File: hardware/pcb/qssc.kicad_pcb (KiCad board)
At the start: 6 copper layers, 210 x 140 mm, 124 parts, among them J1 FT232RL, J10 USB-C, J12 BTB_HOST, J2 5V Barrel, J3 SMA, J4 12V LED, J7 RESET, J8 MW_GATE, J9 JTAG, U1 XC7A35T-1CSG324C, U3 ADF4351BCPZ, U5 GVA-84+, U8 W25Q128JVSIQ, Y1 100MHz TCXO

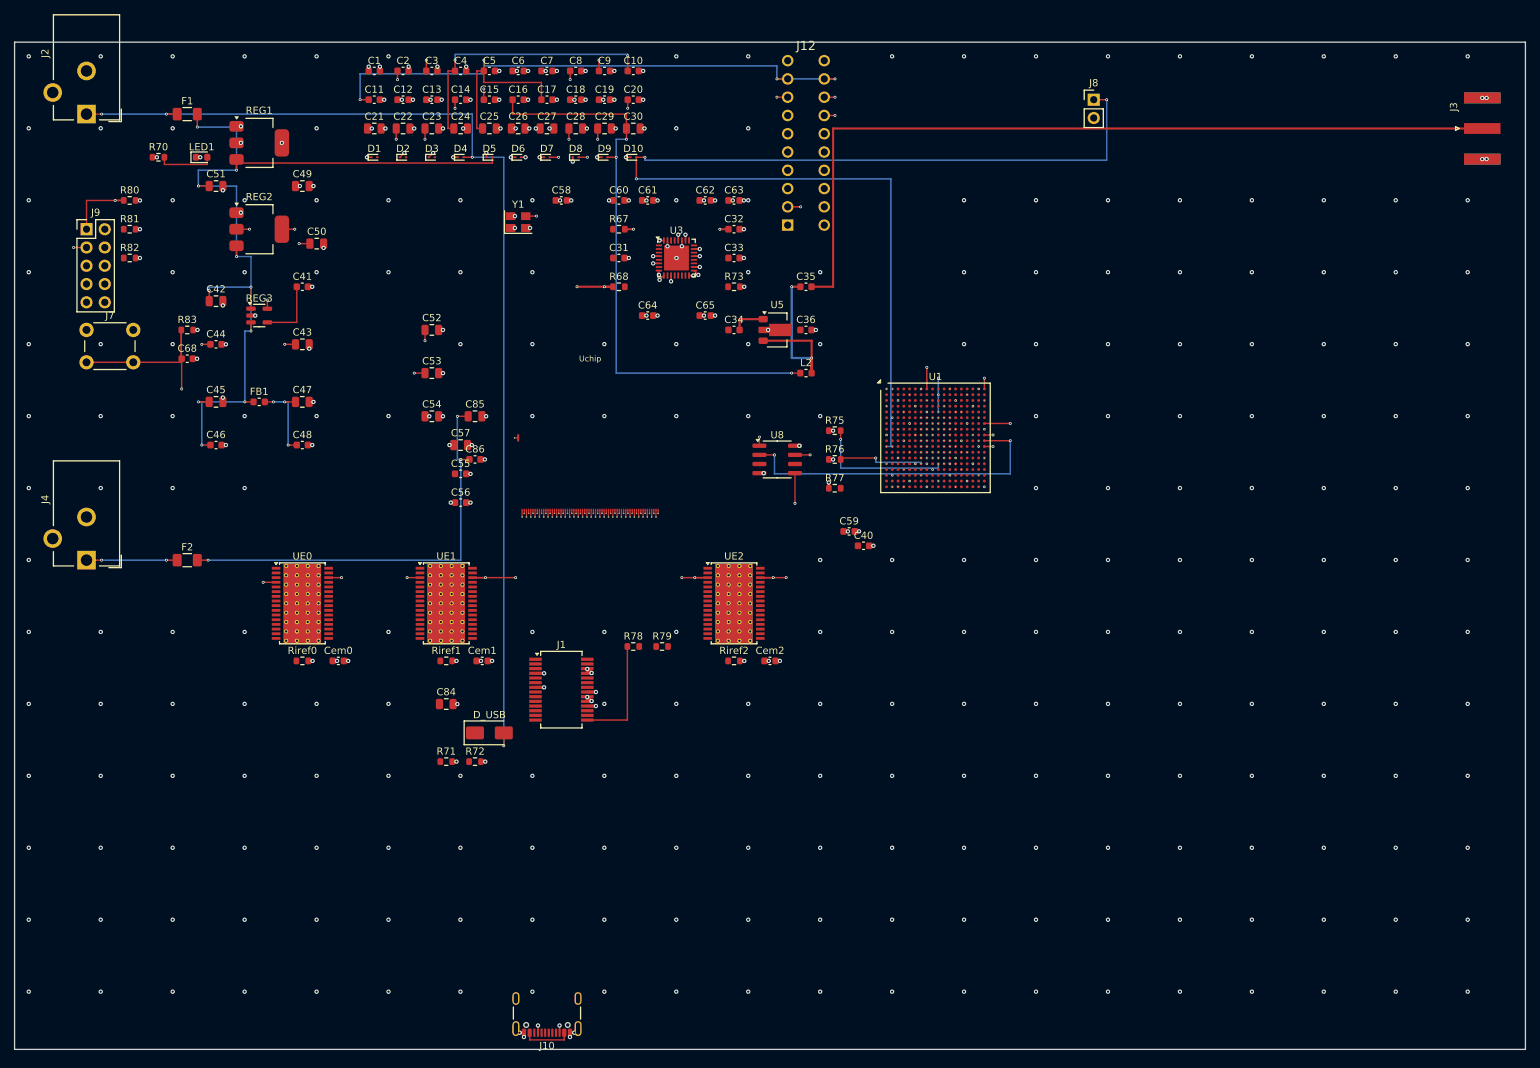
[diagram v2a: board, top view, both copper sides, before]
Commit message: pcb: Ironwood SBT socket + per-datasheet pin fixes + no_connect markers
Step 0 — Ironwood SBT open-top spring-pin socket (emitter face, main board):
  - socket_footprint(): 65 solder pads (64 EM + EM_ANODE) on F.Cu+F.Paste+F.Mask
    at the 0.30mm die-contact pitch, 4 NPTH M2 mount holes, 25x25mm body +
    courtyard. lib_id "qssc:Ironwood_SBT" + symbol; Uchip swapped from
    QSSC_Chip_EM. This is the commercial made-to-order socket that fits the
    20x20mm / 0.30mm-pitch die (no off-the-shelf socket exists at that pitch).
  - Head-board QSSC_Chip_DET (detector face) unchanged: ACF/pogo on B.Cu.

Step 1 — per-datasheet pin audit + (no_connect) emission (addresses
"practically nothing connected per its datasheet"):
  - FT232RL: net pin 24 -> +3V3 (VCC) and pin 23 -> GND (AGND) -- both required
    supply/ground pads per SSOP-28 that were previously unnetted.
  - ADF4351: REFIN- (pin 19) decoupled to GND via new C37 100nF (single-ended
    CMOS ref, datasheet Fig.51); unused RFOUTB+/- (13,14), RFOUTA- (15), SW (5),
    CE (25) declared no_connect per datasheet (unused RF outputs float).
  - add() now takes nc_pins=...; emit_schematic() emits (no_connect) sexps at
    every documented-unused pin: FT232 modem/crystal/LED (12 pins), ADF4351 (5),
    AD7616 parallel-DB bus + SDI/SDOB in 1-wire HW mode (10/chip x4 = 40 head),
    TLC5947 chip2 OUT16-23 + SOUT (9 main).

Both boards: DRC 0/0/0, ERC 0 errors / 0 warnings. 9 PCB tests green.

Co-Authored-By: Claude Code <noreply@anthropic.com>
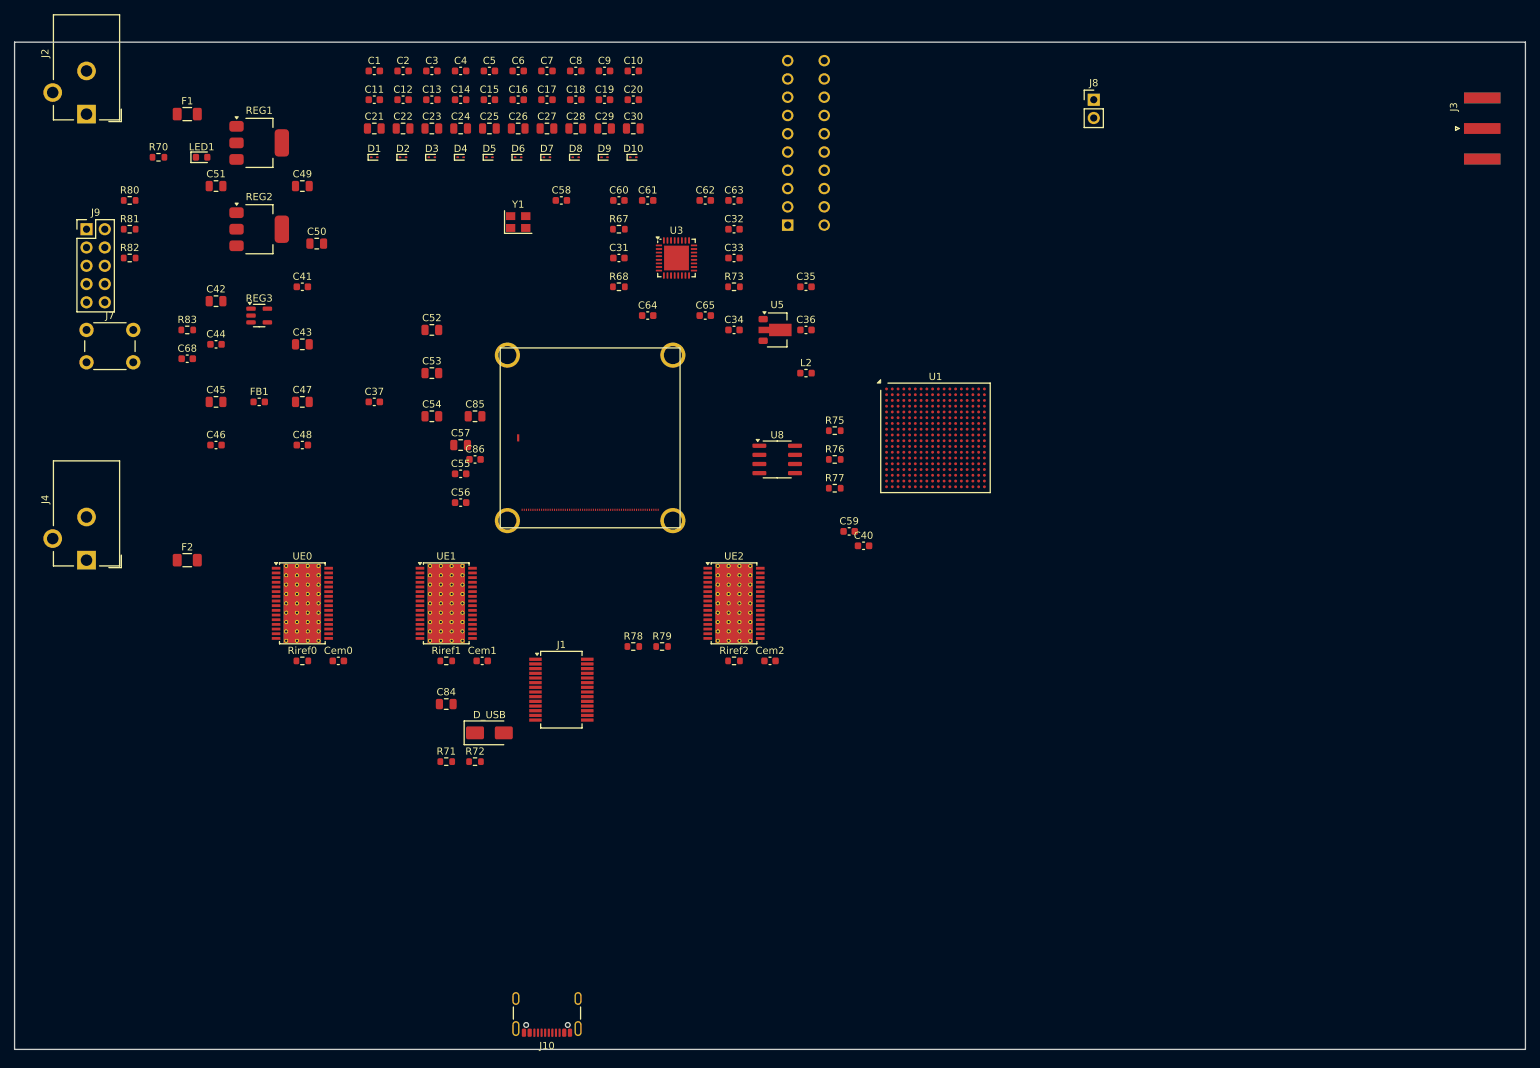
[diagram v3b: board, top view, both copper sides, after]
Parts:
- removed the Uchip at (80.0, 55.0)
- added C37: 100n, C_0603_1608Metric, F.Cu at (50.0, 50.0)
- added Uchip: Ironwood_SBT, qssc:Ironwood_SBT, F.Cu at (80.0, 55.0)
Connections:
- J1 pad 23: (no net) -> GND
- J1 pad 24: (no net) -> +3V3
- U3 pad 19: (no net) -> REFIN_N
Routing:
- net +1V0: track 255.6 -> 0.00 mm, vias 26 -> 0
- net +5V: track 230.7 -> 0.00 mm, vias 14 -> 0
- net +1V8: track 157.6 -> 0.00 mm, vias 16 -> 0
- net TCK: track 154.6 -> 0.00 mm, vias 3 -> 0
- net mw_gate: track 152.2 -> 0.00 mm, vias 4 -> 0
- net +5V_IN: track 150.3 -> 0.00 mm, vias 4 -> 0
- net TDO: track 147.3 -> 0.00 mm, vias 2 -> 0
- net +5V_RF: track 132.4 -> 0.00 mm, vias 8 -> 0
- net reset: track 123.9 -> 0.00 mm, vias 2 -> 0
- net em_xlat: track 121.4 -> 0.00 mm, vias 6 -> 0
- net J3_SIG: track 115.2 -> 0.00 mm
- net em_sin: track 102.5 -> 0.00 mm, vias 2 -> 0
- net em_sclk: track 89.5 -> 0.00 mm, vias 3 -> 0
- net clk_100mhz: track 79.8 -> 0.00 mm, vias 2 -> 0
- net adc_cs2: track 79.7 -> 0.00 mm, vias 2 -> 0
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- removed copper zone on In2.Cu, net +3V3
- removed copper zone on In1.Cu, net GND

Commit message: pcb: verify netlist complete per datasheets, fix C_in/C37 placement short
Connection audit (tools/audit_connections.py) confirms both boards are
netlist-complete and datasheet-correct BEFORE routing:

  - ERC: 0 errors both boards (qssc + chip_module). The 145/203 remaining
    messages are all endpoint_off_grid warnings (authored symbols on a
    non-1.27 mm pin grid) -- cosmetic noise.
  - DRC: 0 violations, 0 unconnected pads, 0 footprint errors both boards.
  - Chip die: 64 emitter_cat -> TLC5947 OUT sinks + EM_ANODE -> +12V_EMIT
    on the main board; 64 DET_IN -> TLV9004 TIA -> AD7616 + DET_REF on the
    head. Every chip net has an off-chip destination (audit confirms).
  - All 268 main-board + head "unnetted" IC pins are intentional spares,
    not missing connections: FPGA 185 spare IO balls (99 power balls all
    netted), AD7616 parallel-DB bus + SDI/SDOB in 1-wire HW serial mode,
    FT232 modem/CBUS pins (USB-only; pin 23 AGND + 24 VCC ARE netted),
    ADF4351 NC pins 5/13/14/15/25 per datasheet, TLC5947 chip2 unused
    OUT16-23 + SOUT, and numberless EP/mount-hole cosmetic pads.

Fix: the main board had 3 DRC violations (shorting_items +5V_IN/ADF_TEMP,
courtyards_overlap, solder_mask_bridge) all from ONE root cause -- the new
input-bulk cap C_in and the ADF4351 TEMP decoupler C37 both fell through
assign_pcb_positions()'s else-branch to the (50,50) default cell, so
C_in.1 (+5V_IN) overlapped C37.1 (ADF_TEMP). Give both explicit placements
in the fixed dict (C_in @46,8 near the barrel jack; C37 @104,36 below U3).
Regenerated both boards -> DRC 0/0/0.

route_signals.py: the chip-net force-fail referenced an undefined
`structured_chip` (NameError if run). Define it as an empty set so the
file is runnable and all chip nets are cleanly deferred to the future
_structured_bus_fanout (task #36) / FreeRouting -- routing stays paused
per the user's instruction until the netlist was verified.

Adds tools/audit_connections.py (per-datasheet pin/rail/chip audit) a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
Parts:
- added C_in: 10uF, C_0805_2012Metric, F.Cu at (46.0, 8.00)
- moved C37 55.8 mm to (104.0, 36.0)
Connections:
- net REFIN_N renamed ADF_TEMP
- U3 pad : (no net) -> GND
- UE0 pad : (no net) -> GND
- UE1 pad : (no net) -> GND
- UE2 pad : (no net) -> GND

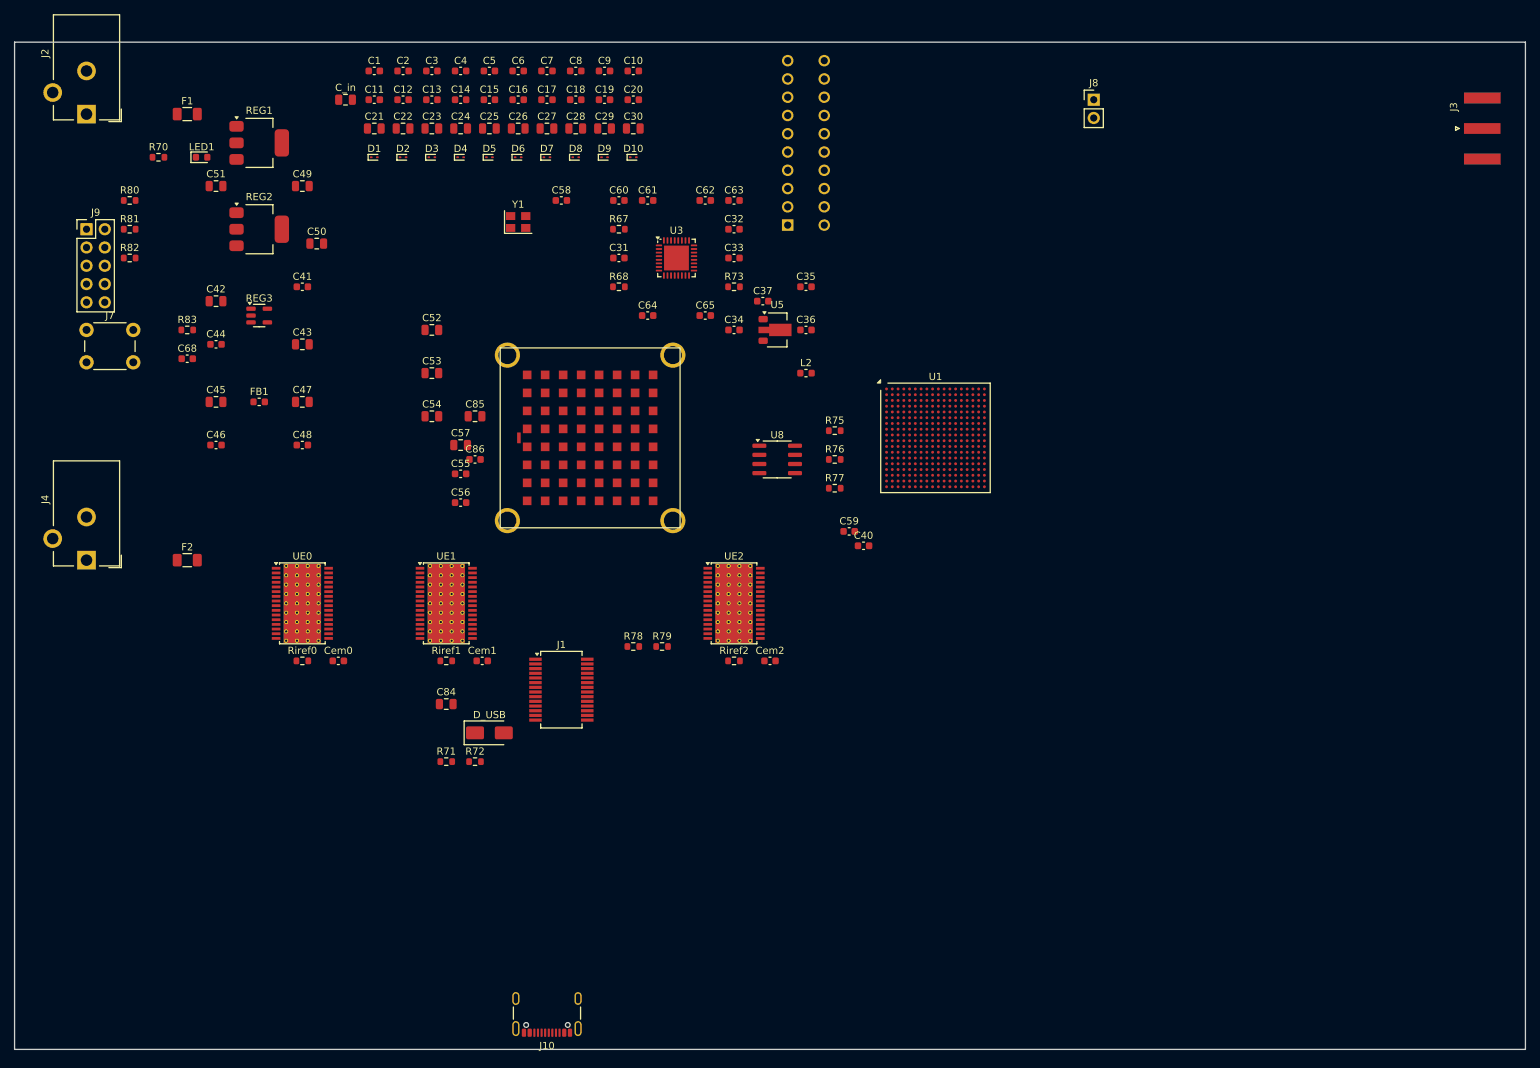
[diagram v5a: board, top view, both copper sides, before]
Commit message: route: make _chip_fanout a no-op for the 2.5 mm 8x8 die grid (FreeRouting escapes)
The 8x8 die electrode grid is 2.5 mm pitch (1.2 mm pads, 1.3 mm inter-pad
gaps) -- COARSE, not the 0.30 mm fine pitch the staggered dog-bone fanout was
written for. Applying that dog-bone geometry to an INTERIOR 8x8 grid shorts
neighbouring nets: each pad's per-pad escape direction (nearest die edge) lands
its 0.5/1.0 mm stub+via on the adjacent-row pad -> DRC shorting_items between
emitter_cat{i} and emitter_cat{i+8} (68 shorts main / 98 head after routing).

At 2.5 mm pitch a 0.2 mm track escapes each pad directly through the 1.3 mm
gaps, so no dog-bone vias are needed. _chip_fanout is now a no-op (returns the
empty 5-tuple); the 64 die nets stay bare and force-failed in the line router,
and FreeRouting escapes the 8x8 grid directly -- a standard autorouter job at
this pitch. Verified: both boards DRC 0 violations after route_signals
(was 68/98 shorting_items). Die nets (64 emitter_cat / 64 DET_IN+DET_TIA) +
signal nets remain unrouted, pending the FreeRouting pass.

Co-Authored-By: Claude Code <noreply@anthropic.com>
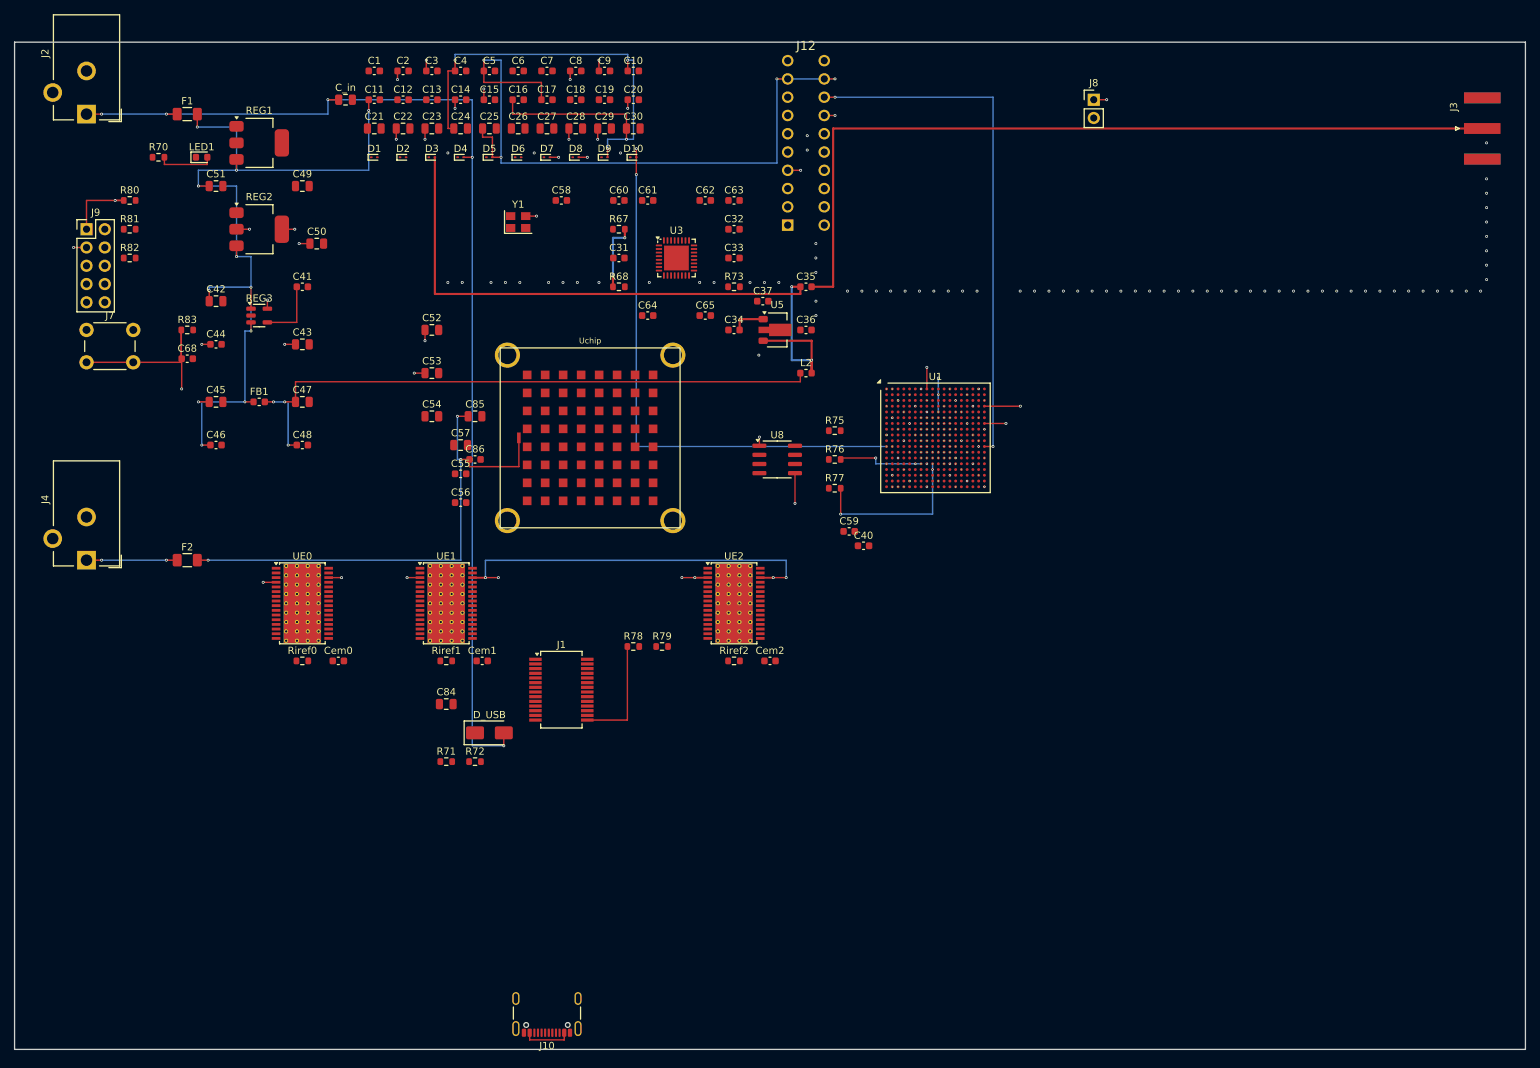
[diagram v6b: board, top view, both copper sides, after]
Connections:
- U3 pad : GND -> (no net)
- UE0 pad : GND -> (no net)
- UE1 pad : GND -> (no net)
- UE2 pad : GND -> (no net)
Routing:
- net +1V0: track 0.00 -> 255.6 mm, vias 0 -> 26
- net +5V: track 0.00 -> 218.3 mm, vias 0 -> 15
- net +5V_RF: track 0.00 -> 163.7 mm, vias 0 -> 7
- net +1V8: track 0.00 -> 157.6 mm, vias 0 -> 16
- net +5V_IN: track 0.00 -> 155.8 mm, vias 0 -> 5
- net TCK: track 0.00 -> 154.6 mm, vias 0 -> 3
- net mw_gate: track 0.00 -> 153.4 mm, vias 0 -> 4
- net TDO: track 0.00 -> 147.3 mm, vias 0 -> 2
- net reset: track 0.00 -> 123.9 mm, vias 0 -> 2
- net em_xlat: track 0.00 -> 116.6 mm, vias 0 -> 6
- net J3_SIG: track 0.00 -> 115.2 mm
- net em_sin: track 0.00 -> 102.5 mm, vias 0 -> 2
- net RF_AMP_OUT: track 0.00 -> 98.0 mm, vias 0 -> 2
- net em_sclk: track 0.00 -> 89.5 mm, vias 0 -> 3
- net clk_100mhz: track 0.00 -> 80.6 mm, vias 0 -> 2
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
